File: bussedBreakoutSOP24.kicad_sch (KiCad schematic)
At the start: 46 parts, among them J1 Conn_01x12_Pin, J10 Conn_01x06_Pin, J11 Conn_01x06_Pin, J12 Conn_01x06_Pin, J13 Conn_01x06_Pin, J14 Conn_01x06_Pin, J15 Conn_01x06_Pin, J16 Conn_01x06_Pin, J17 Conn_01x06_Pin, J18 Conn_01x06_Pin, J19 Conn_01x06_Pin, J2 Conn_01x01_Pin, J20 Conn_01x06_Pin, J21 Conn_01x12_Pin, J22 Conn_01x20_Pin, J23 Conn_01x20_Pin, J24 Conn_01x20_Pin, J25 Conn_01x20_Pin, J26 Conn_01x20_Pin, J27 Conn_01x20_Pin, J28 Conn_01x20_Pin, J29 Conn_01x20_Pin, J3 Conn_01x01_Pin, J30 Conn_01x20_Pin, J31 Conn_01x20_Pin, J32 Conn_01x12_Pin, J4 Conn_01x05_Pin, J5 Conn_01x05_Pin, J6 Conn_01x01_Pin, J7 Conn_01x01_Pin, J8 Conn_01x12_Pin, J9 Conn_01x06_Pin

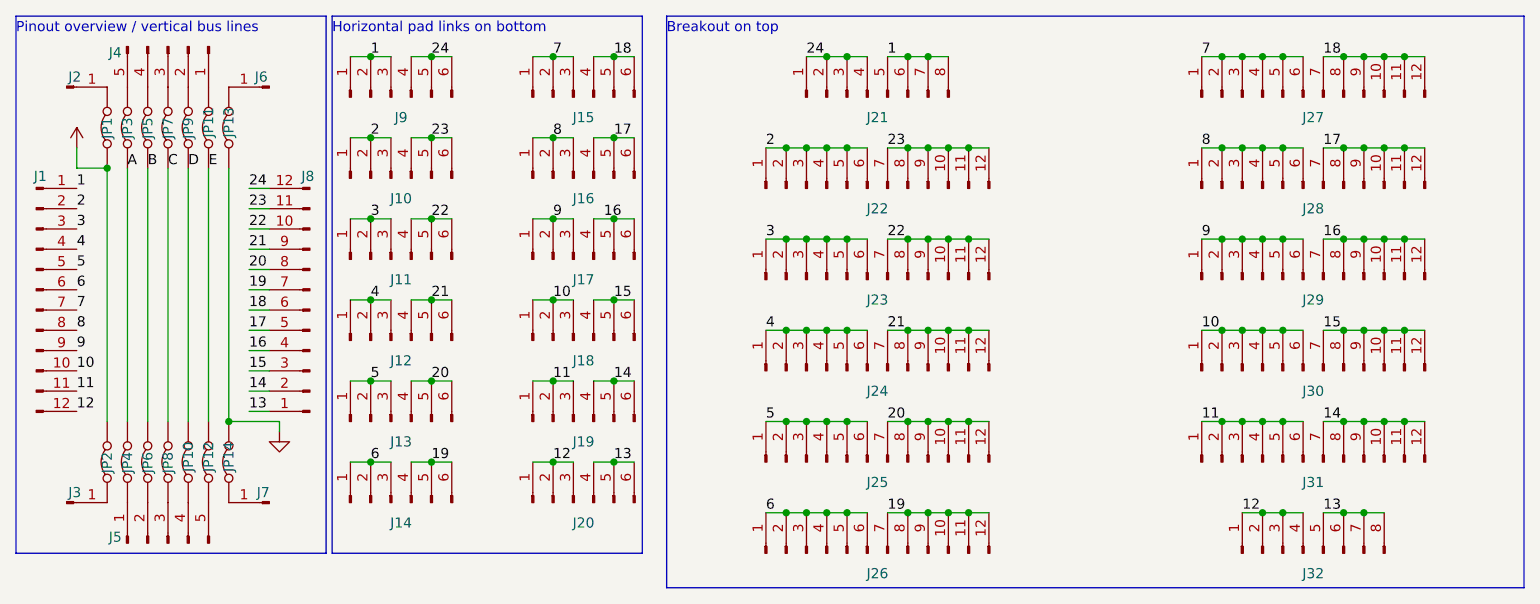
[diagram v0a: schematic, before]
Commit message: Change to a SOP24 breakout
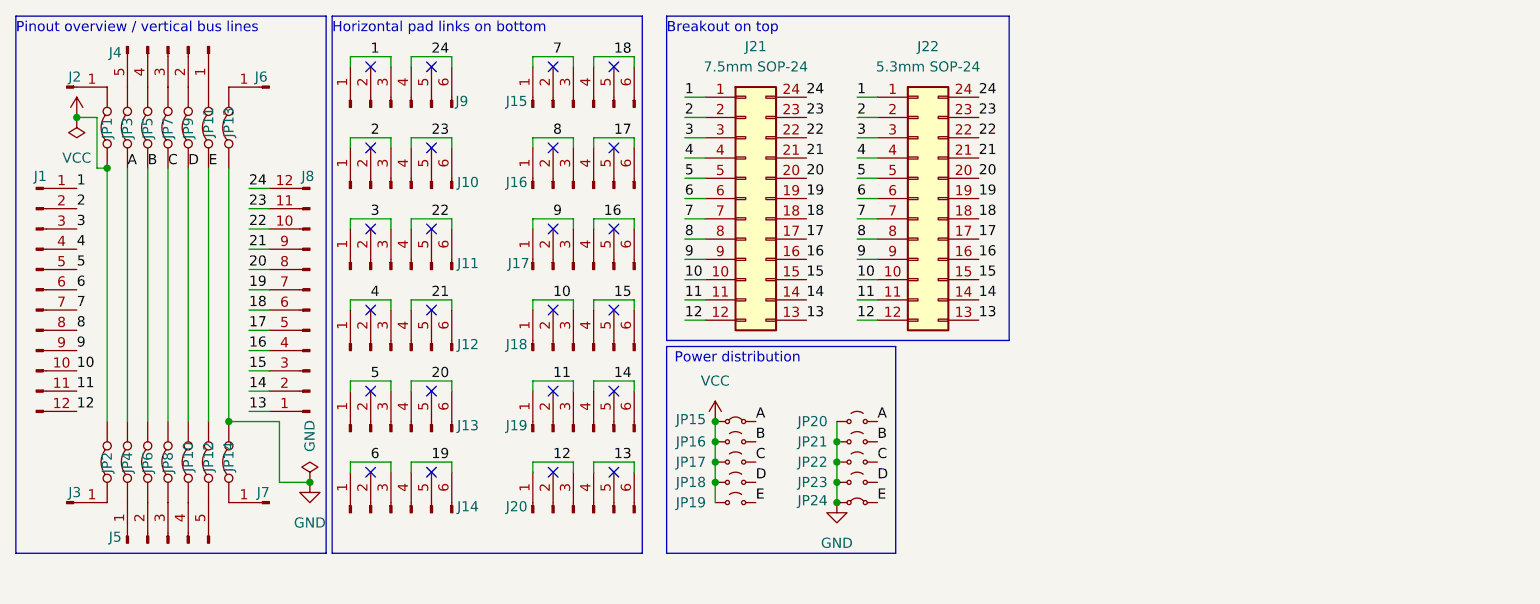
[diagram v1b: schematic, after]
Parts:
- removed J21, J32: Conn_01x12_Pin, SMD:SMD_0805_grid_1x6_interleaved_0402_1x2, symbol Connector:Conn_01x08_Pin
- removed J22, J23, J24, J25, J26, J27, J28, J29, J30, J31: Conn_01x20_Pin, SMD:SMD_0805_grid_1x6_interleaved_0402_2x2, symbol Connector:Conn_01x12_Pin
- added J21: 7.5mm SOP-24, Package_SO:SOP-24_7.5x15.4mm_P1.27mm, symbol Connector_Generic:Conn_02x12_Counter_Clockwise
- added J22: 5.3mm SOP-24, Package_SO:SO-24_5.3x15mm_P1.27mm, symbol Connector_Generic:Conn_02x12_Counter_Clockwise
- added JP15, JP24: Jumper_2_Small_Bridged, SMD:SolderJumper-2_0402_Bridged_Unmarked, symbol Jumper:Jumper_2_Small_Bridged
- added JP16, JP17, JP18, JP19, JP20, JP21, JP22, JP23: Jumper_2_Small_Open, SMD:SolderJumper-2_0402_Open_Unmarked, symbol Jumper:Jumper_2_Small_Open
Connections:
- net 1: now also J21.1 (Pin_1), J22.1 (Pin_1); no longer J9.2 (Pin_2)
- net 10: now also J21.10 (Pin_10), J22.10 (Pin_10); no longer J18.2 (Pin_2)
- net 11: now also J21.11 (Pin_11), J22.11 (Pin_11); no longer J19.2 (Pin_2)
- net 12: now also J21.12 (Pin_12), J22.12 (Pin_12); no longer J20.2 (Pin_2)
- net 13: now also J21.13 (Pin_13), J22.13 (Pin_13); no longer J20.5 (Pin_5)
- net 14: now also J21.14 (Pin_14), J22.14 (Pin_14); no longer J19.5 (Pin_5)
- net 15: now also J21.15 (Pin_15), J22.15 (Pin_15); no longer J18.5 (Pin_5)
- net 16: now also J21.16 (Pin_16), J22.16 (Pin_16); no longer J17.5 (Pin_5)
- net 17: now also J21.17 (Pin_17), J22.17 (Pin_17); no longer J16.5 (Pin_5)
- net 18: now also J21.18 (Pin_18), J22.18 (Pin_18); no longer J15.5 (Pin_5)
- net 19: now also J21.19 (Pin_19), J22.19 (Pin_19); no longer J14.5 (Pin_5)
- net 2: now also J21.2 (Pin_2), J22.2 (Pin_2); no longer J10.2 (Pin_2)
- net 20: now also J21.20 (Pin_20), J22.20 (Pin_20); no longer J13.5 (Pin_5)
- net 21: now also J21.21 (Pin_21), J22.21 (Pin_21); no longer J12.5 (Pin_5)
- net 22: now also J21.22 (Pin_22), J22.22 (Pin_22); no longer J11.5 (Pin_5)
- net 23: now also J21.23 (Pin_23), J22.23 (Pin_23); no longer J10.5 (Pin_5)
- net 24: now also J21.24 (Pin_24), J22.24 (Pin_24); no longer J9.5 (Pin_5)
- net 3: now also J21.3 (Pin_3), J22.3 (Pin_3); no longer J11.2 (Pin_2)
- net 4: now also J21.4 (Pin_4), J22.4 (Pin_4); no longer J12.2 (Pin_2)
- net 5: now also J21.5 (Pin_5), J22.5 (Pin_5); no longer J13.2 (Pin_2)
- net 6: now also J21.6 (Pin_6), J22.6 (Pin_6); no longer J14.2 (Pin_2)
- net 7: now also J21.7 (Pin_7), J22.7 (Pin_7); no longer J15.2 (Pin_2)
- net 8: now also J21.8 (Pin_8), J22.8 (Pin_8); no longer J16.2 (Pin_2)
- net 9: now also J21.9 (Pin_9), J22.9 (Pin_9); no longer J17.2 (Pin_2)
- net A: now also JP15.2 (B), JP20.2 (B)
- net B: now also JP16.2 (B), JP21.2 (B)
- net C: now also JP17.2 (B), JP22.2 (B)
- net D: now also JP18.2 (B), JP23.2 (B)
- net E: now also JP19.2 (B), JP24.2 (B)
- net GND: now also JP20.1 (A), JP21.1 (A), JP22.1 (A), JP23.1 (A), JP24.1 (A)
- net VCC: now also JP15.1 (A), JP16.1 (A), JP17.1 (A), JP18.1 (A), JP19.1 (A)
- no-connect marks 0 -> 24
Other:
- note added: "Power distribution"
- moved on the sheet: J10, J11, J12, J13, J14, J15, J16, J17, J18, J19, J20, J9

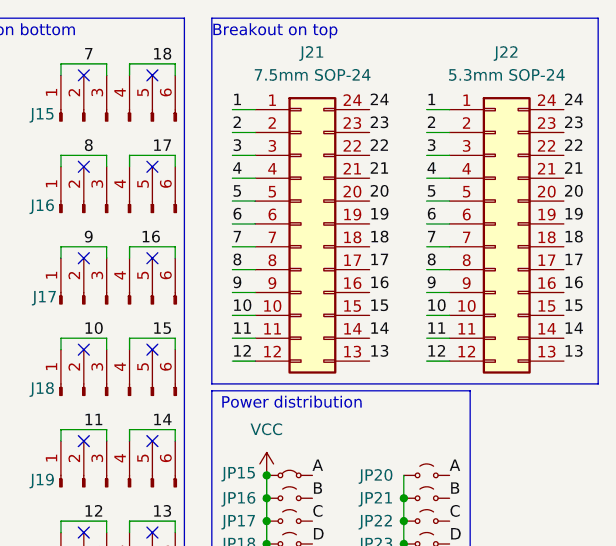
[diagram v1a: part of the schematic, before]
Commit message: Change to a custom SOP-24 footprint accomodating the narrowest 3.9mm to the widest 7.5mm SO-24 packages
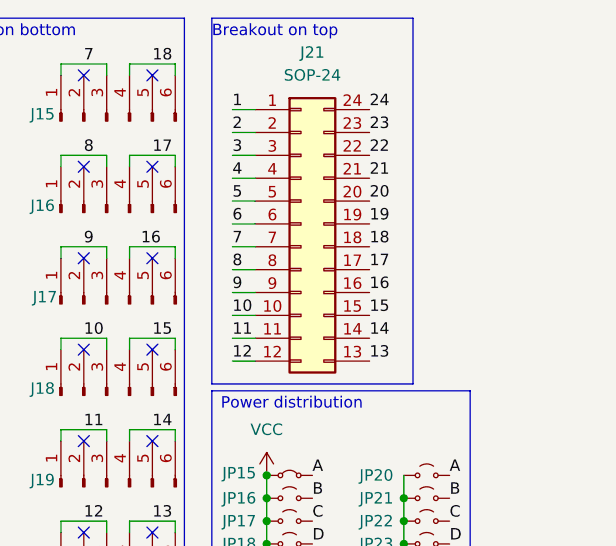
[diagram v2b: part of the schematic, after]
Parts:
- removed J22: 5.3mm SOP-24, Package_SO:SO-24_5.3x15mm_P1.27mm, symbol Connector_Generic:Conn_02x12_Counter_Clockwise
- J21: value 7.5mm SOP-24 -> SOP-24; footprint Package_SO:SOP-24_7.5x15.4mm_P1.27mm -> SMD:SOP-24_3.9-7.5mmx15.4mm_P1.27mm
